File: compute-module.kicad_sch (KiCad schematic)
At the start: 112 parts, among them J201 DF40HC(3.0)-100DS-0.4v, J202 DF40HC(3.0)-100DS-0.4v, M201 compute-module-4-1.5mm, Q201 PJE138K, Q202 SSM3J332R, Q203 SSM3J332R, Q204 SSM3J332R, Q205 SSM3J332R, Q206 PJE138K, Q207 PJE138K, Q208 PJE138K, Q209 PJE138K, Q210 PJE138K, U201 TXB0104_UQFN, U202 NTS0104_DHVQFN, U203 TXB0104_UQFN, U204 MCP23017T-E_QFN

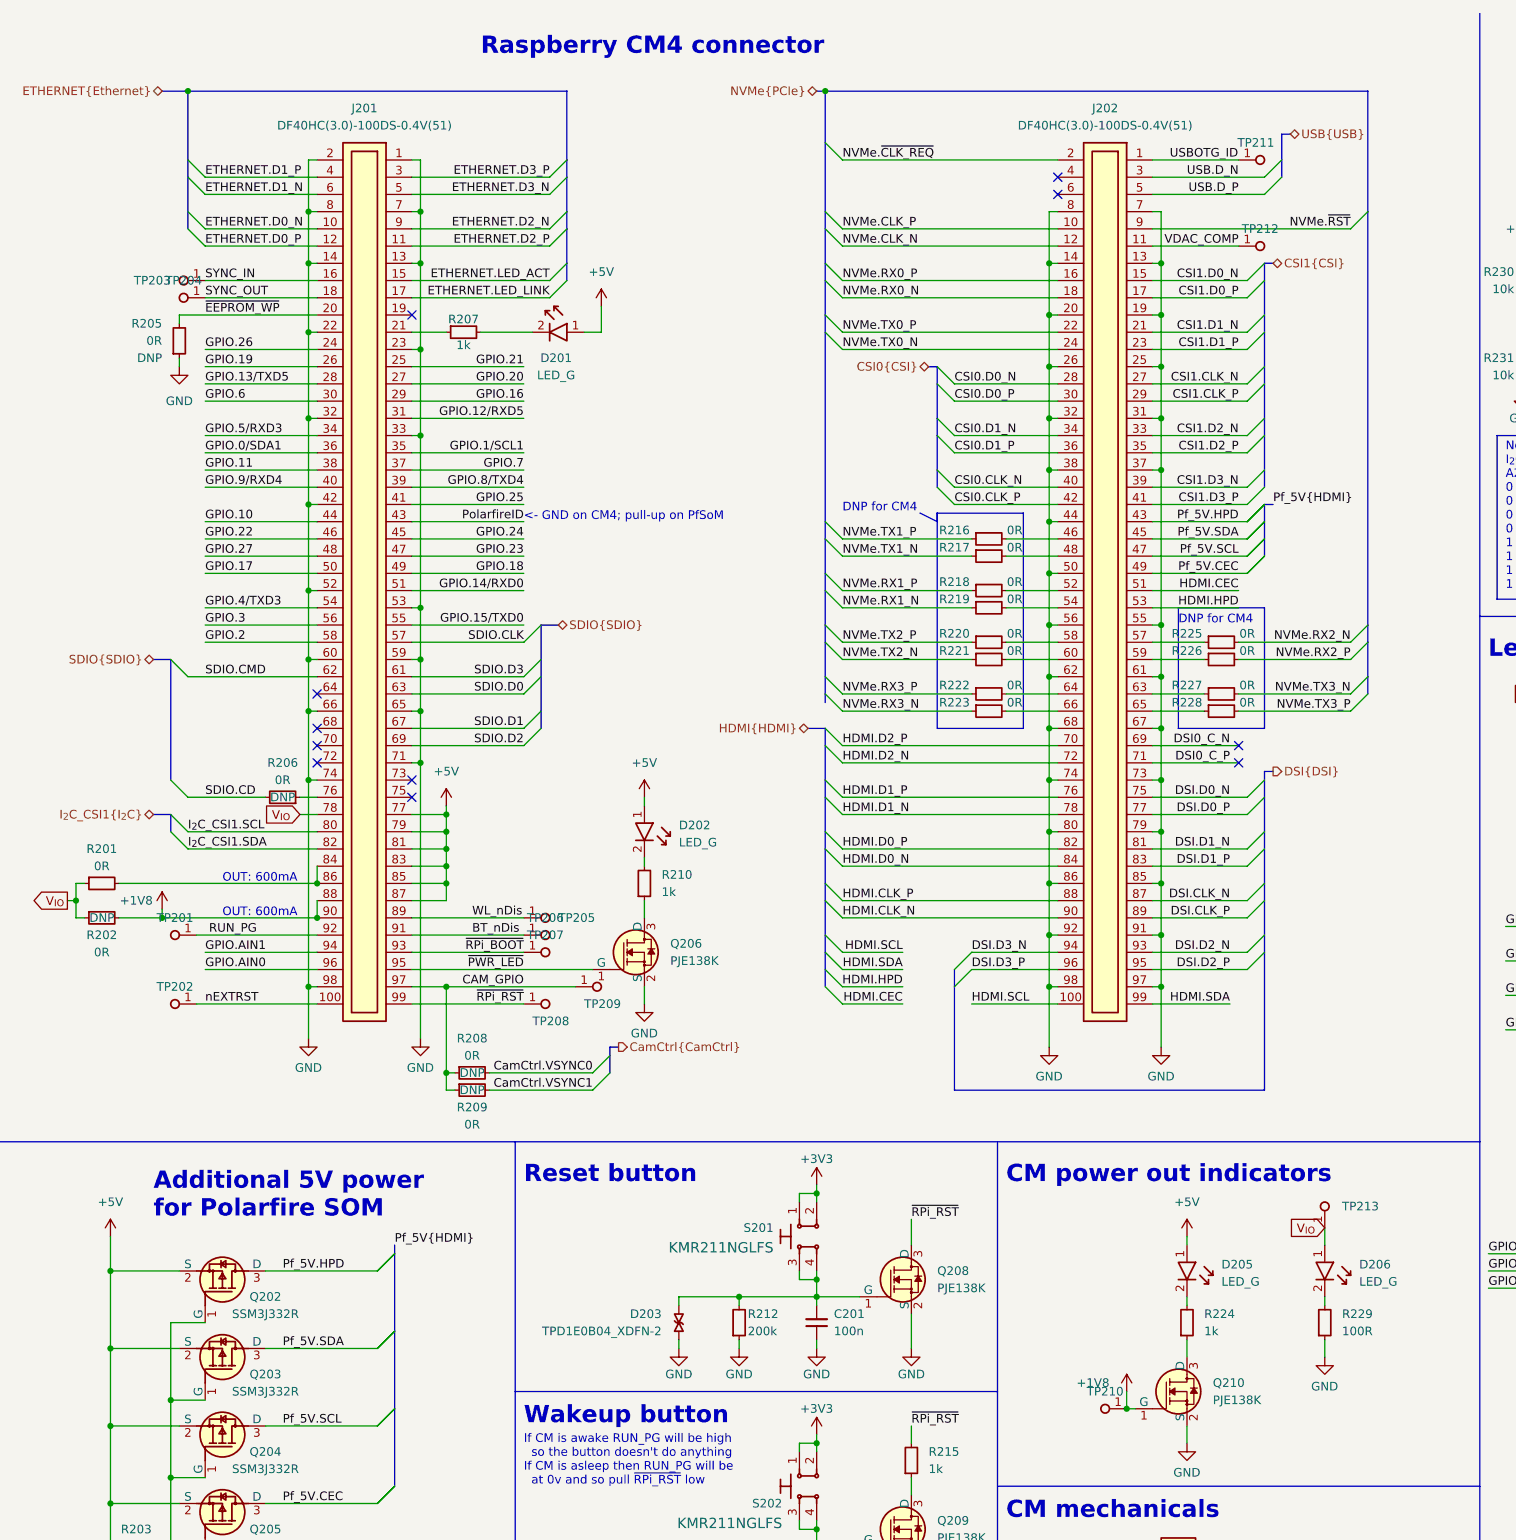
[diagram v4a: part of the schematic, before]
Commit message: [#55181] PCB: NVMe disc: placement and HS routing; minor related changes in sch
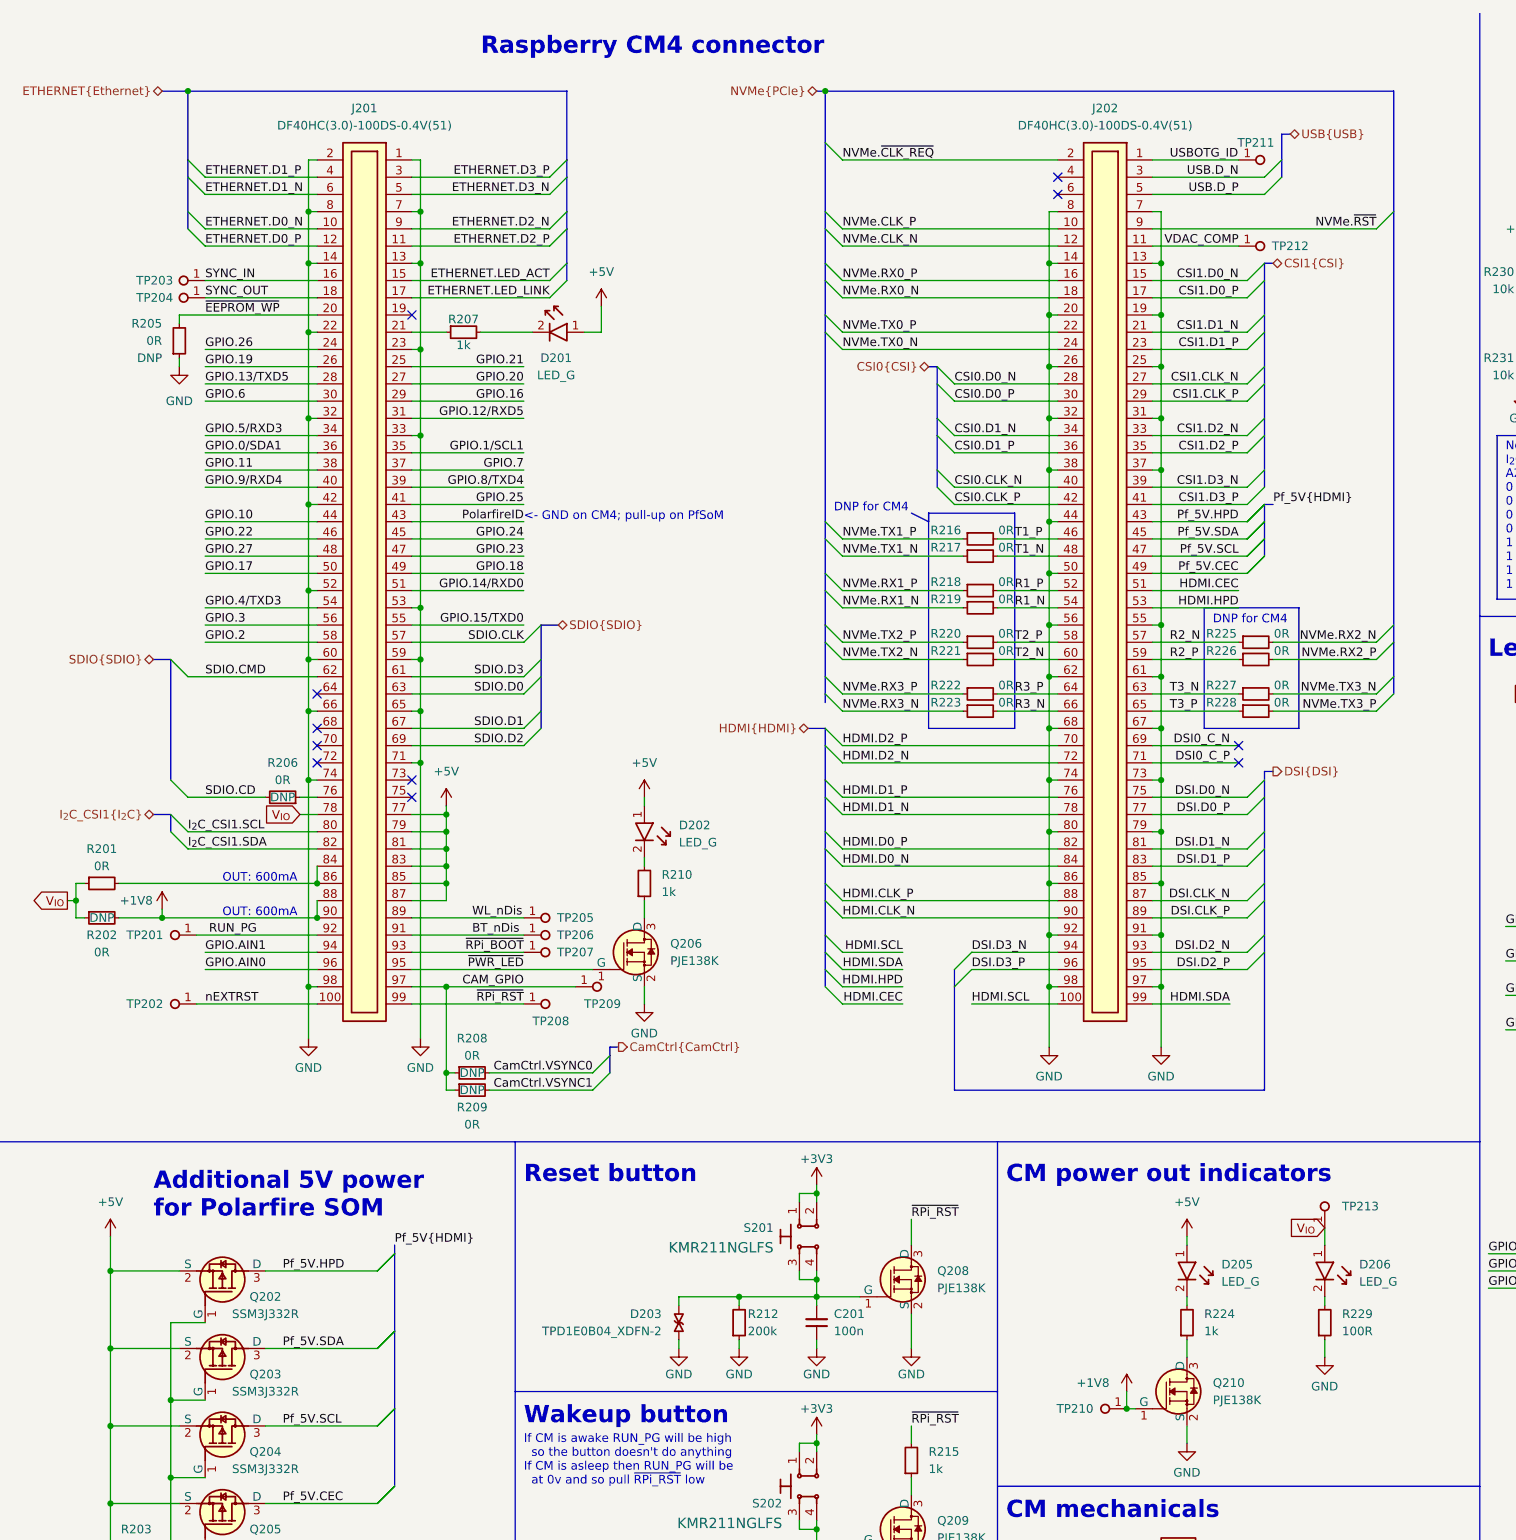
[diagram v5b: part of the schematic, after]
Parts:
- R216, R217, R218, R219, R220, R221, R222, R223, R225, R226, R227, R228: footprint antmicro-footprints:R_0402_1005Metric -> antmicro-footprints:R_0201; symbol antmicroResistors0402:R_0R_0402 -> antmicroResistorsmisc:R_0R_0201; MPN ERJ2GE0R00X -> CR0201-FX-0R00GLF; Manufacturer Panasonic -> Bourns; Tolerance (none) -> 1%
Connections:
- net T1_P: now reaches J202.46, R216.2
- net T1_N: now reaches J202.48, R217.2
- net R1_P: now reaches J202.52, R218.2
- net R1_N: now reaches J202.54, R219.2
- net R2_N: now reaches J202.57, R225.1
- net T2_P: now reaches J202.58, R220.2
- net R2_P: now reaches J202.59, R226.1
- net T2_N: now reaches J202.60, R221.2
- net T3_N: now reaches J202.63, R227.1
- net R3_P: now reaches J202.64, R222.2
- net T3_P: now reaches J202.65, R228.1
- net R3_N: now reaches J202.66, R223.2
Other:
- moved on the sheet: R216, R217, R218, R219, R220, R221, R222, R223, R225, R226, R227, R228

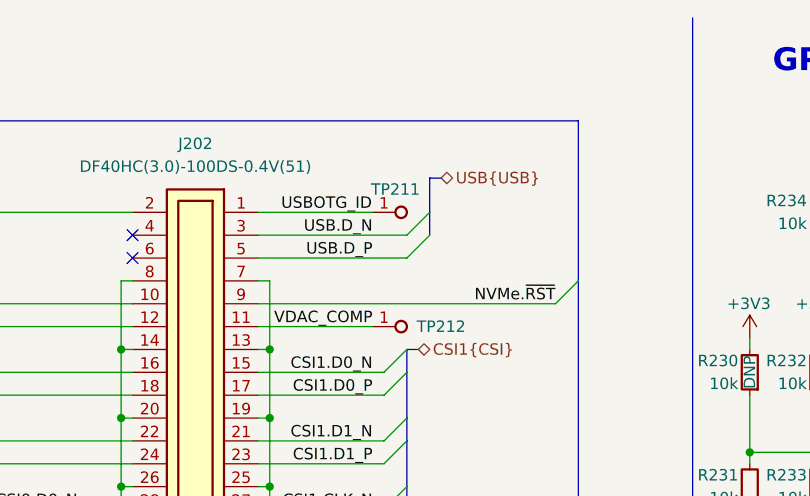
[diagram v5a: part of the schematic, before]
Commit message: [#55247] Change USB schematic: Remove PD from App USB, add CC controller
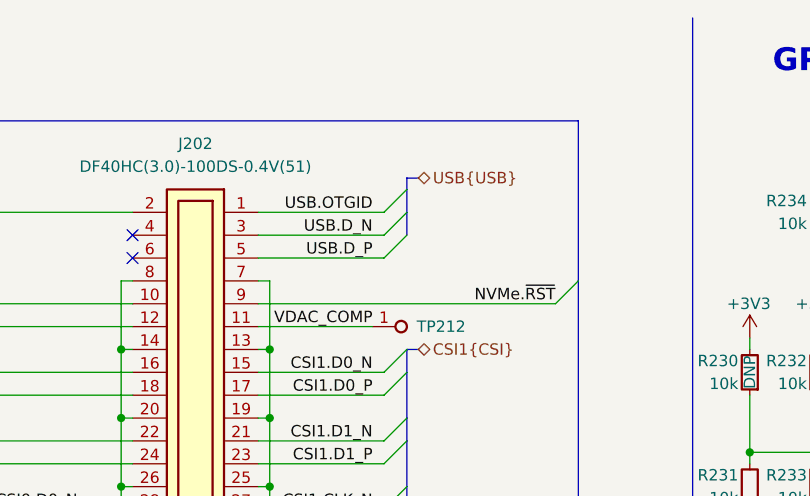
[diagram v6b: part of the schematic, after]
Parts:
- removed TP211: TP_1mm_SMD, antmicro-footprints:TP_SMD_0.75mm, symbol antmicroTestPoints:TP_0.75mm_SMD
- R216, R217, R218, R219, R220, R221, R222, R223, R225, R226, R227, R228: value R_0R_0402 -> R_0R_0201
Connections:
- net USBOTG_ID renamed USB.OTGID

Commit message: [#55181] PCB: USB placement; Sch: minor USB related changes
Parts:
- added Q211: PJE138K, antmicro-footprints:SOT-523, symbol antmicroTransistorsFETsMOSFETsSingle:PJE138K
- added Q212: SSM3J332R, antmicro-footprints:SOT-23-3, symbol antmicroTransistorsFETsMOSFETsSingle:SSM3J332R
- added R260, R261: R_100k_0402, antmicro-footprints:R_0402_1005Metric, symbol antmicroResistors0402:R_100k_0402
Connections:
- net GND: now also Q211.2 (S), R260.1
- net GPIO.17: now also Q212.3 (D)
- net PolarfireID: now also Q211.1 (G), R260.2
- new net: Q211.3 (D), Q212.1 (G), R261.1
- new net USBA_VBUS: Q212.2 (S), R261.2
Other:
- note added: "V_{BUS} connection for Polarfire SOM"
- note added: "V_{BUS} on Polarfire ->"

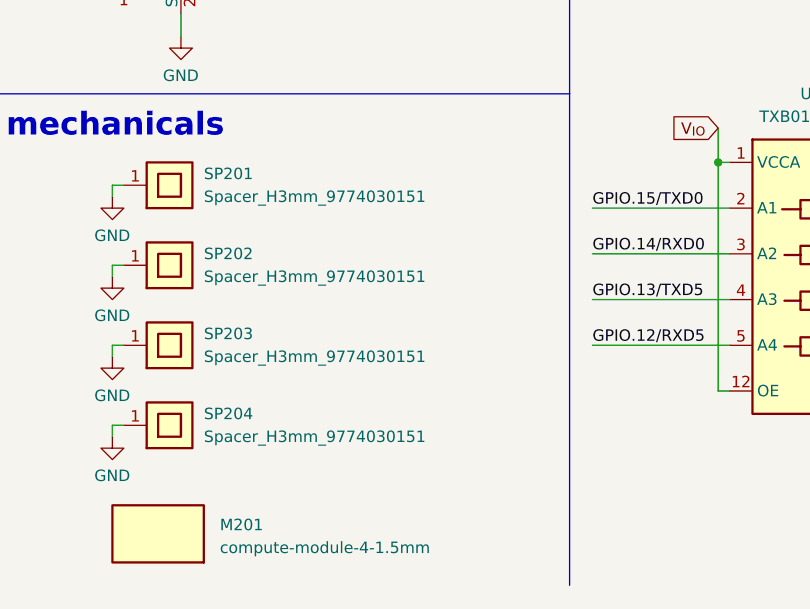
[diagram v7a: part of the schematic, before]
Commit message: [#55181] Change adapter spacer to 2mm; update spacers from lib
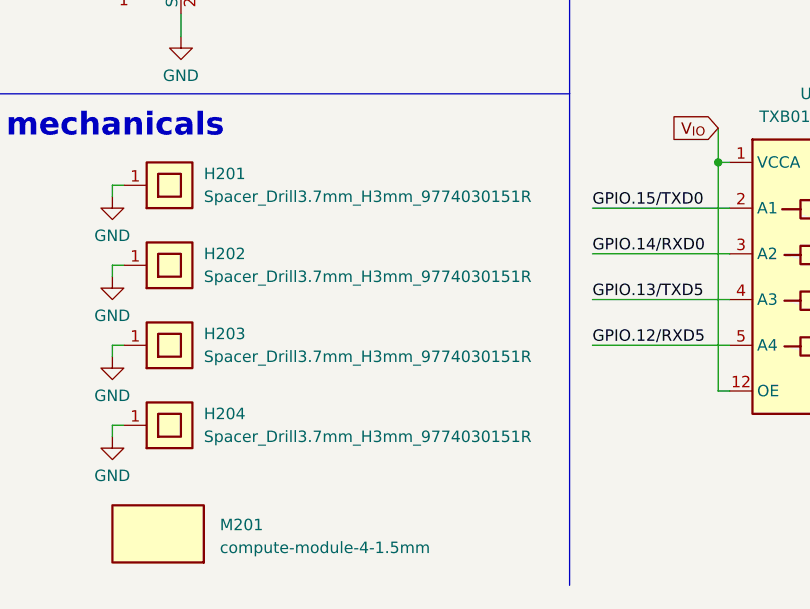
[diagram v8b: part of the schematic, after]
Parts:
- H201: renamed from SP201; value Spacer_H3mm_9774030151 -> Spacer_Drill3.7mm_H3mm_9774030151R
- H202: renamed from SP202; value Spacer_H3mm_9774030151 -> Spacer_Drill3.7mm_H3mm_9774030151R
- H203: renamed from SP203; value Spacer_H3mm_9774030151 -> Spacer_Drill3.7mm_H3mm_9774030151R
- H204: renamed from SP204; value Spacer_H3mm_9774030151 -> Spacer_Drill3.7mm_H3mm_9774030151R
